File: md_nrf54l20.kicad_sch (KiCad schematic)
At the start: 42 parts, among them J1 U.FL Conn, J10 Conn_01x15, J5 USB_C, J7 JST SH I2C, J9 Conn_01x15, SW1 RESET, U1 nRF54L20, U2 MCP1700x-280xxTT, U3 CH347T, U5 MLD-TF PUSH-H18, Y1 8MHz, Y2 32MHz

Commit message: Routing
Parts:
- removed C10, C9: 10uF, Capacitor_SMD:C_0805_2012Metric, symbol Device:C
- removed J1: U.FL Conn, Connector_Coaxial:U.FL_Hirose_U.FL-R-SMT-1_Vertical, symbol Connector:Conn_Coaxial_Small
- removed U2: MCP1700x-280xxTT, Package_TO_SOT_SMD:SOT-23, symbol Regulator_Linear:MCP1700x-280xxTT
- added C17, C18: 1uF, Capacitor_SMD:C_0402_1005Metric, symbol Device:C
- added J2: Conn_01x04, md-l20B:Chip Antenna AANI-CH-0070, symbol Connector_Generic:Conn_01x04
- added R13: 10k, Resistor_SMD:R_0402_1005Metric, symbol Device:R
- added R4, R5, R7: 0, Resistor_SMD:R_0402_1005Metric, symbol Device:R
- added U4: AP2112K-3.3, Package_TO_SOT_SMD:SOT-23-5, symbol Regulator_Linear:AP2112K-3.3
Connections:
- net +3V3: now also C18.1, U4.5 (VOUT)
- net GND: now also C17.2, C18.2, J2.2 (Pin_2), J2.4 (Pin_4), R4.2, R5.2, U4.2 (GND)
- net VBUS: now also C17.1, U4.1 (VIN), U4.3 (EN)
- net ANT: now reaches U1.34 (ANT)
- net ANT: now also R4.1, R7.2
- new net: J2.1 (Pin_1), J2.3 (Pin_3), R5.1, R7.1
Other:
- moved on the sheet: C11, D1, R6

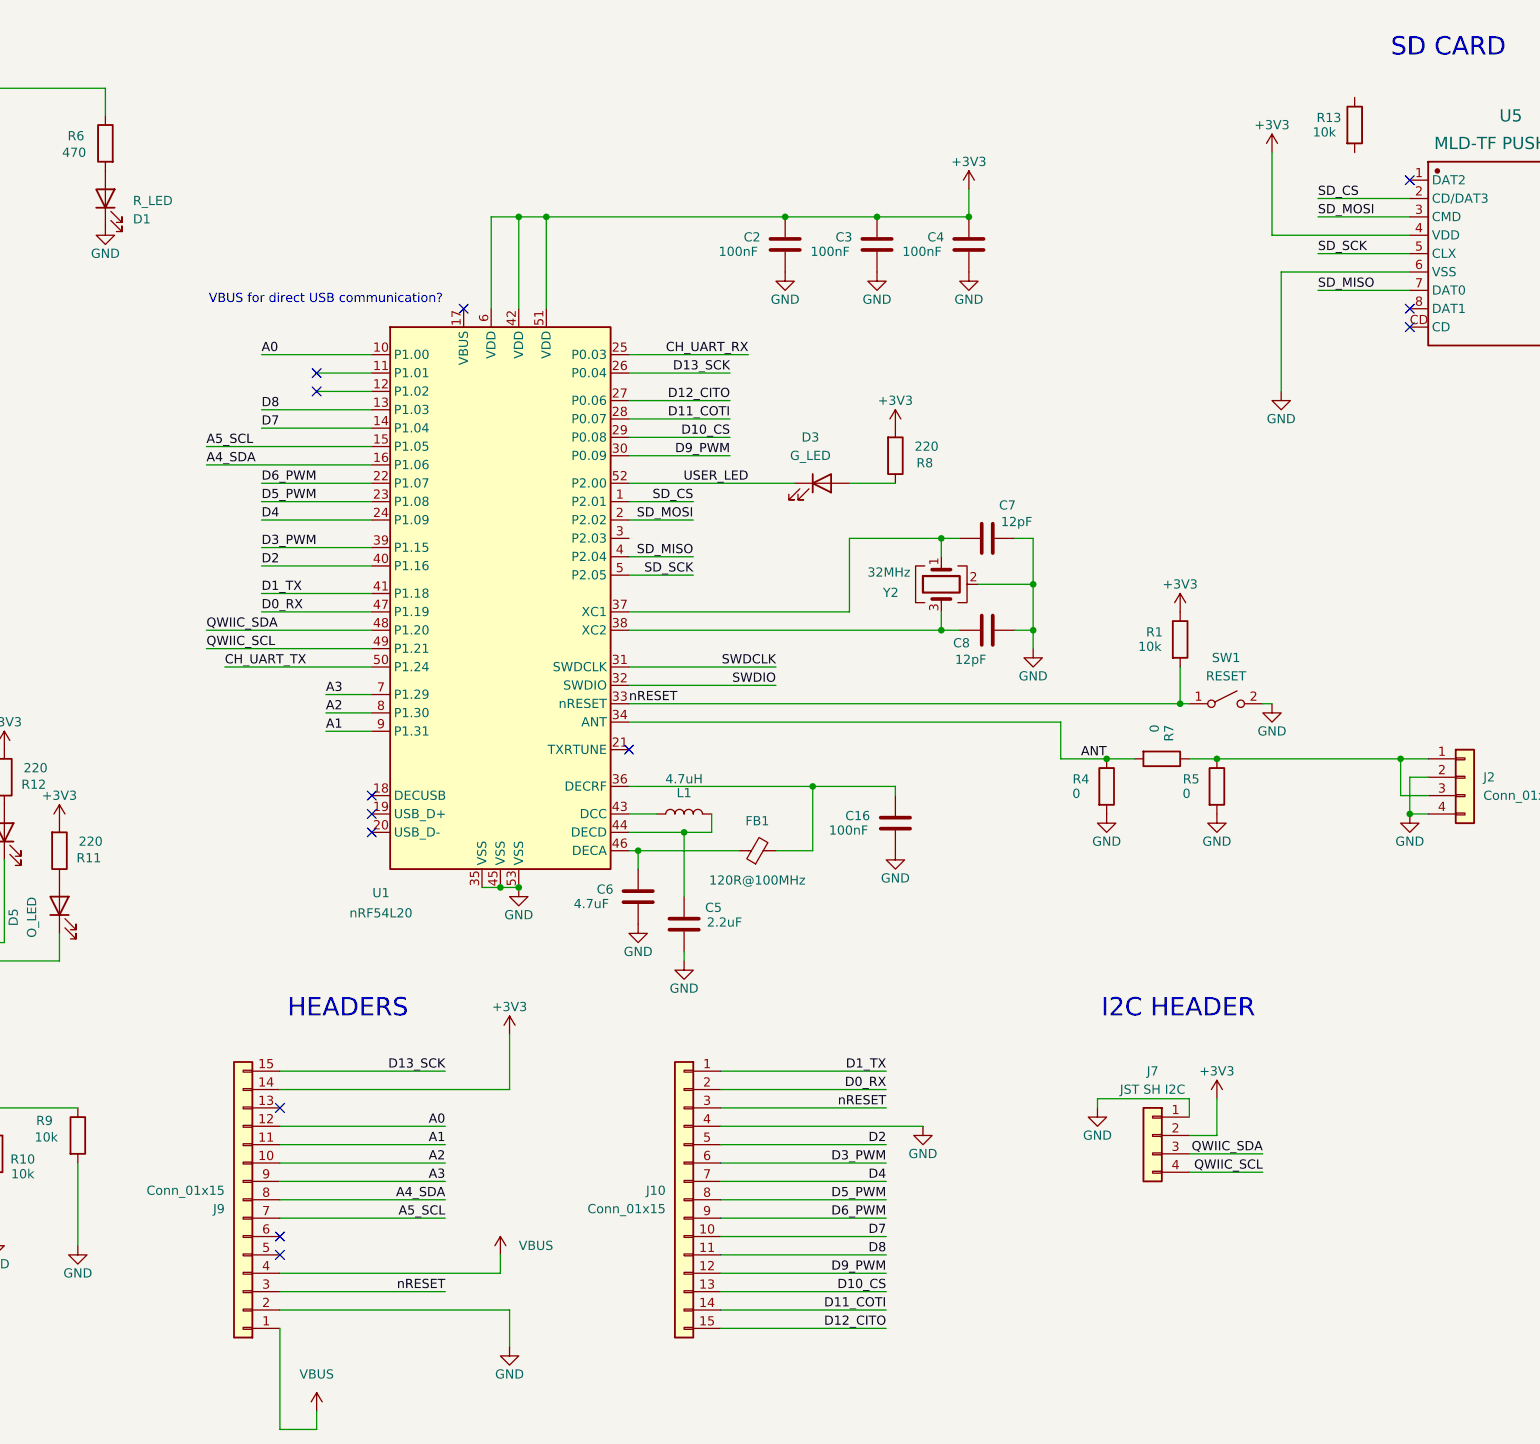
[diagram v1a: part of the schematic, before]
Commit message: Mirrored headers, swapping
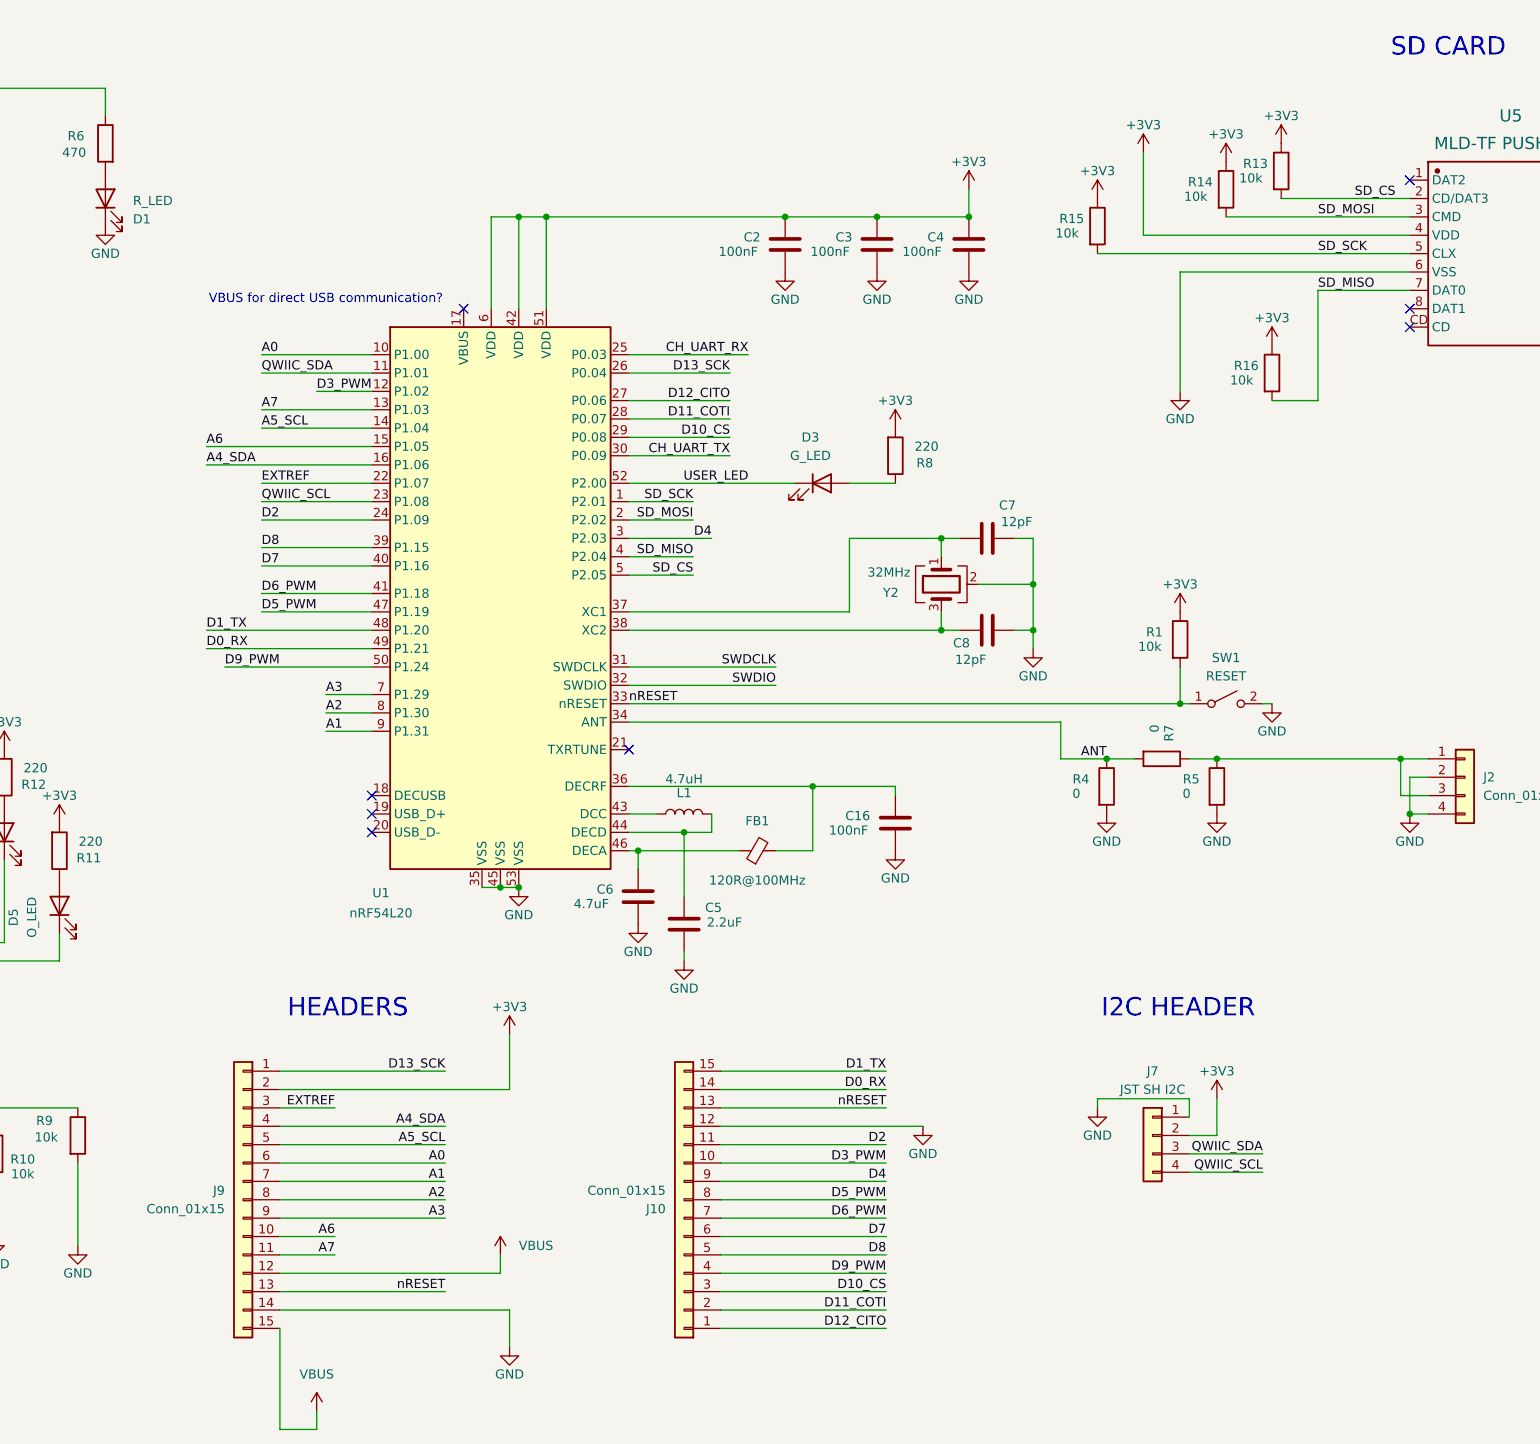
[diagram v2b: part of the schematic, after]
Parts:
- added R14, R15, R16: 10k, Resistor_SMD:R_0402_1005Metric, symbol Device:R
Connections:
- net +3V3: now also J9.2 (Pin_2), R13.1, R14.1, R15.1, R16.1; no longer J9.14 (Pin_14)
- net A0: now also J9.6 (Pin_6); no longer J9.12 (Pin_12)
- net A1: now also J9.7 (Pin_7); no longer J9.11 (Pin_11)
- net A2: now also J9.8 (Pin_8); no longer J9.10 (Pin_10)
- net A4_SDA: now also J9.4 (Pin_4); no longer J9.8 (Pin_8)
- net A5_SCL: now also J9.5 (Pin_5), U1.14 (P1.04); no longer J9.7 (Pin_7), U1.15 (P1.05)
- net CH_UART_TX: now also U1.30 (P0.09); no longer U1.50 (P1.24)
- net D0_RX: now also J10.14 (Pin_14), U1.49 (P1.21); no longer J10.2 (Pin_2), U1.47 (P1.19)
- net D10_CS: now also J10.3 (Pin_3); no longer J10.13 (Pin_13)
- net D11_COTI: now also J10.2 (Pin_2); no longer J10.14 (Pin_14)
- net D12_CITO: now also J10.1 (Pin_1); no longer J10.15 (Pin_15)
- net D13_SCK: now also J9.1 (Pin_1); no longer J9.15 (Pin_15)
- net D1_TX: now also J10.15 (Pin_15), U1.48 (P1.20); no longer J10.1 (Pin_1), U1.41 (P1.18)
- net D2: now also J10.11 (Pin_11), U1.24 (P1.09); no longer J10.5 (Pin_5), U1.40 (P1.16)
- net D3_PWM: now also J10.10 (Pin_10), U1.12 (P1.02); no longer J10.6 (Pin_6), U1.39 (P1.15)
- net D4: now also J10.9 (Pin_9), U1.3 (P2.03); no longer J10.7 (Pin_7), U1.24 (P1.09)
- net D5_PWM: now also U1.47 (P1.19); no longer U1.23 (P1.08)
- net D6_PWM: now also J10.7 (Pin_7), U1.41 (P1.18); no longer J10.9 (Pin_9), U1.22 (P1.07)
- net D7: now also J10.6 (Pin_6), U1.40 (P1.16); no longer J10.10 (Pin_10), U1.14 (P1.04)
- net D8: now also J10.5 (Pin_5), U1.39 (P1.15); no longer J10.11 (Pin_11), U1.13 (P1.03)
- net D9_PWM: now also J10.4 (Pin_4), U1.50 (P1.24); no longer J10.12 (Pin_12), U1.30 (P0.09)
- net GND: now also J10.12 (Pin_12), J9.14 (Pin_14); no longer J10.4 (Pin_4), J9.2 (Pin_2)
- net QWIIC_SCL: now also U1.23 (P1.08); no longer U1.49 (P1.21)
- net QWIIC_SDA: now also U1.11 (P1.01); no longer U1.48 (P1.20)
- net SD_CS: now also R13.2, U1.5 (P2.05); no longer U1.1 (P2.01)
- net SD_MISO: now also R16.2
- net SD_MOSI: now also R14.2
- net SD_SCK: now also U1.1 (P2.01), R15.2; no longer U1.5 (P2.05)
- net VBUS: now also J9.12 (Pin_12), J9.15 (Pin_15); no longer J9.1 (Pin_1), J9.4 (Pin_4)
- net nRESET: now also J10.13 (Pin_13), J9.13 (Pin_13); no longer J10.3 (Pin_3), J9.3 (Pin_3)
- new net A6: J9.10 (Pin_10), U1.15 (P1.05)
- new net A7: J9.11 (Pin_11), U1.13 (P1.03)
- new net EXTREF: J9.3 (Pin_3), U1.22 (P1.07)
- no-connect marks 22 -> 17
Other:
- moved on the sheet: J10, J9, R13

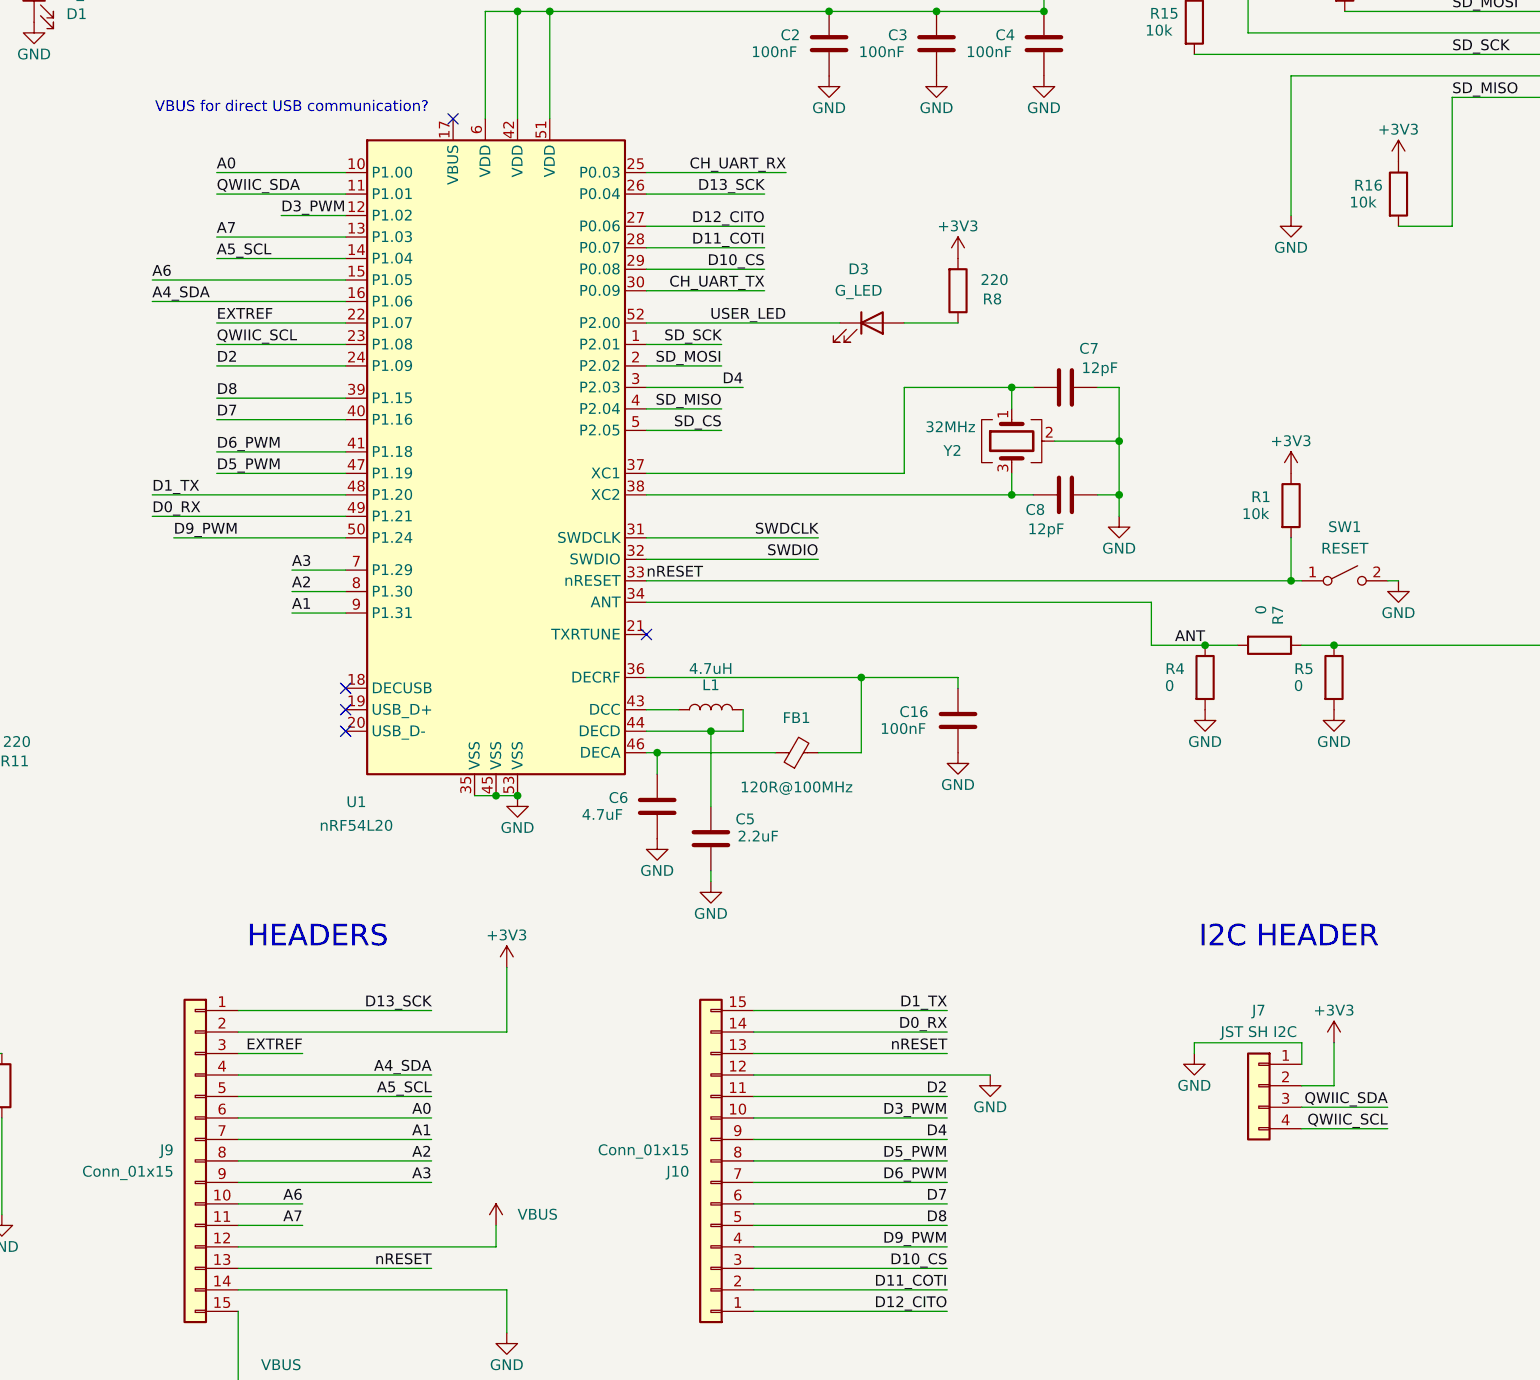
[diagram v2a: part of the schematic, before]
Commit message: Analog header swap, start digital
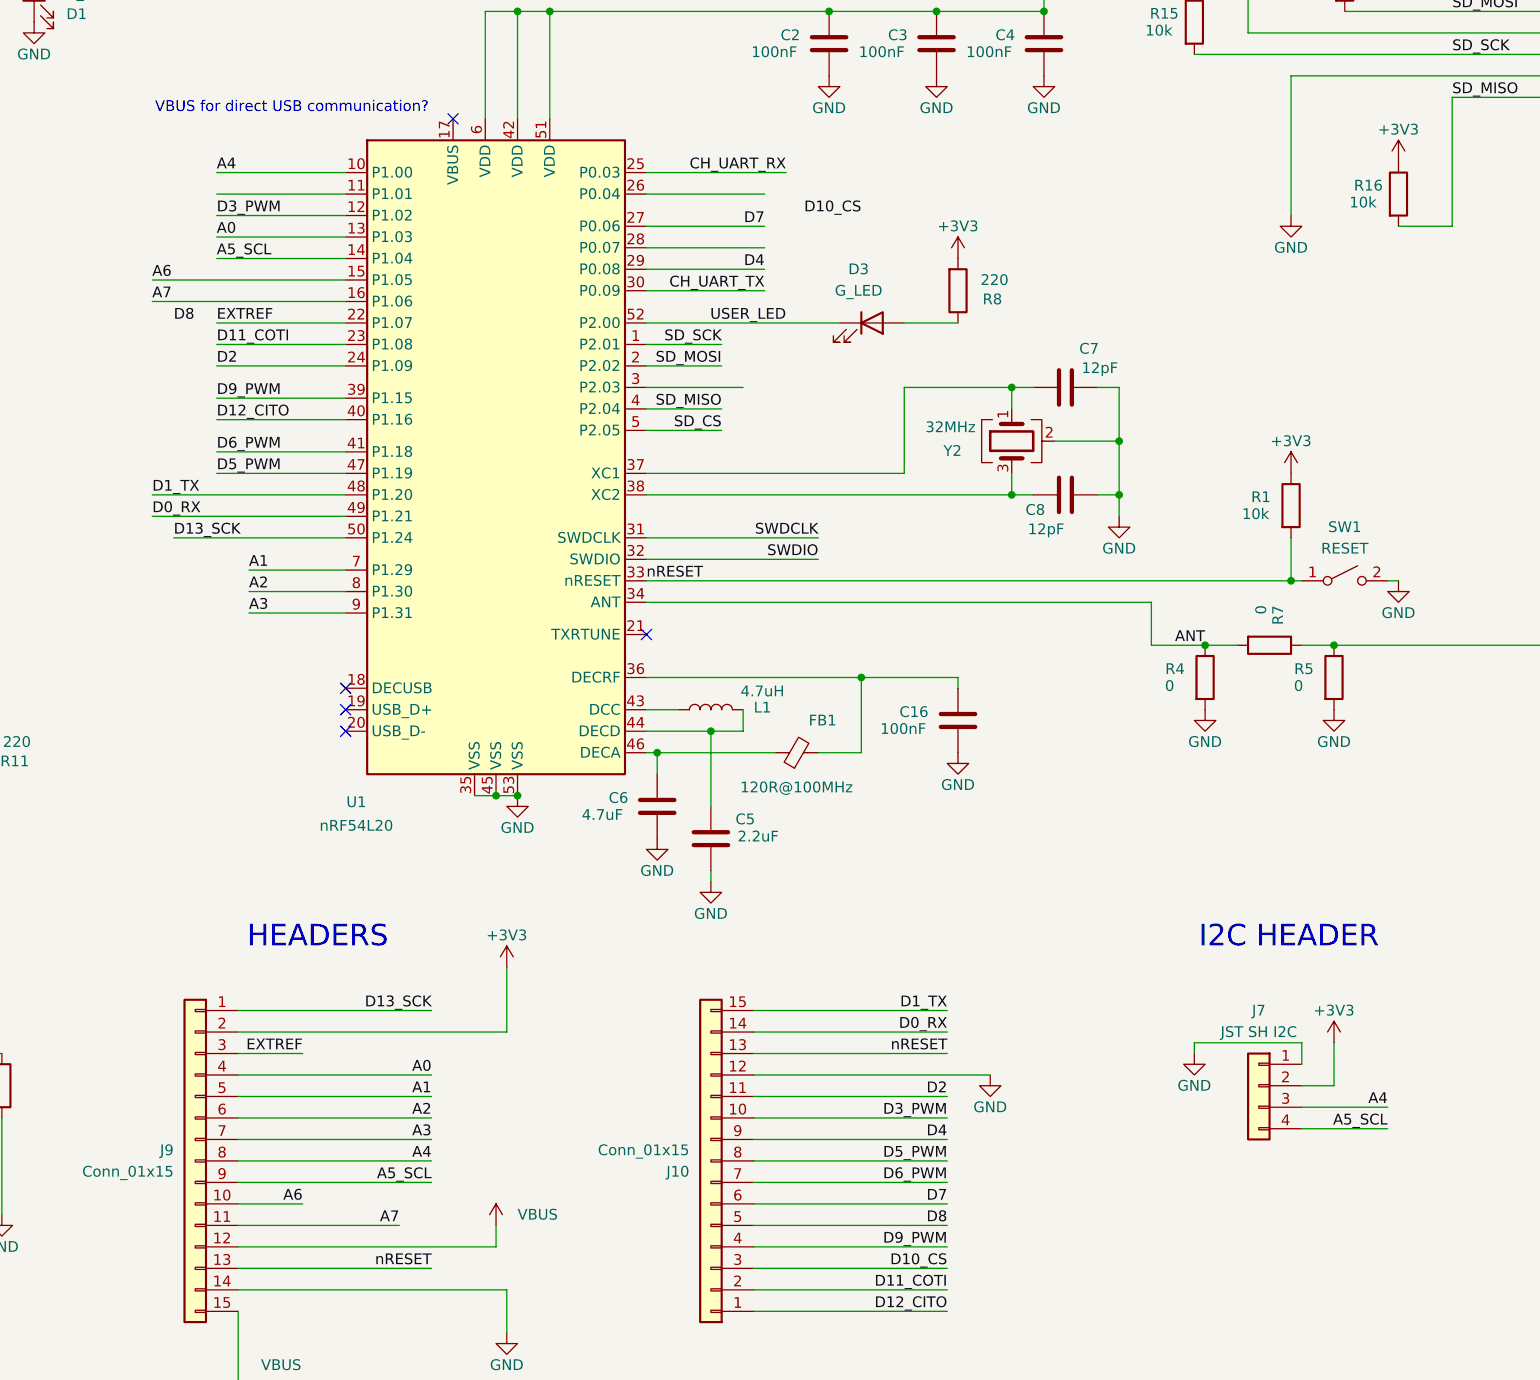
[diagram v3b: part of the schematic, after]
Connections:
- net A0: now also J9.4 (Pin_4), U1.13 (P1.03); no longer J9.6 (Pin_6), U1.10 (P1.00)
- net A1: now also J9.5 (Pin_5), U1.7 (P1.29); no longer J9.7 (Pin_7), U1.9 (P1.31)
- net A2: now also J9.6 (Pin_6); no longer J9.8 (Pin_8)
- net A3: now also J9.7 (Pin_7), U1.9 (P1.31); no longer J9.9 (Pin_9), U1.7 (P1.29)
- net A5_SCL: now also J7.4 (Pin_4), J9.9 (Pin_9); no longer J9.5 (Pin_5)
- net A7: now also U1.16 (P1.06); no longer U1.13 (P1.03)
- net D10_CS: no longer U1.29 (P0.08)
- net D11_COTI: now also U1.23 (P1.08); no longer U1.28 (P0.07)
- net D12_CITO: now also U1.40 (P1.16); no longer U1.27 (P0.06)
- net D13_SCK: now also U1.50 (P1.24); no longer U1.26 (P0.04)
- net D4: now also U1.29 (P0.08); no longer U1.3 (P2.03)
- net D7: now also U1.27 (P0.06); no longer U1.40 (P1.16)
- net D8: no longer U1.39 (P1.15)
- net D9_PWM: now also U1.39 (P1.15); no longer U1.50 (P1.24)
- removed net A4_SDA: J9.4 (Pin_4), U1.16 (P1.06)
- removed net QWIIC_SCL: J7.4 (Pin_4), U1.23 (P1.08)
- net QWIIC_SDA: no longer names the net of U1.11 (P1.01)
- net QWIIC_SDA: no longer J7.3 (Pin_3)
- new net A4: J7.3 (Pin_3), J9.8 (Pin_8), U1.10 (P1.00)
